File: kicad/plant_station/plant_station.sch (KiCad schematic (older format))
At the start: 20 parts, among them IC1 LP5024RSMR, IC2 VEML7700-TT, U1 NodeMCU2

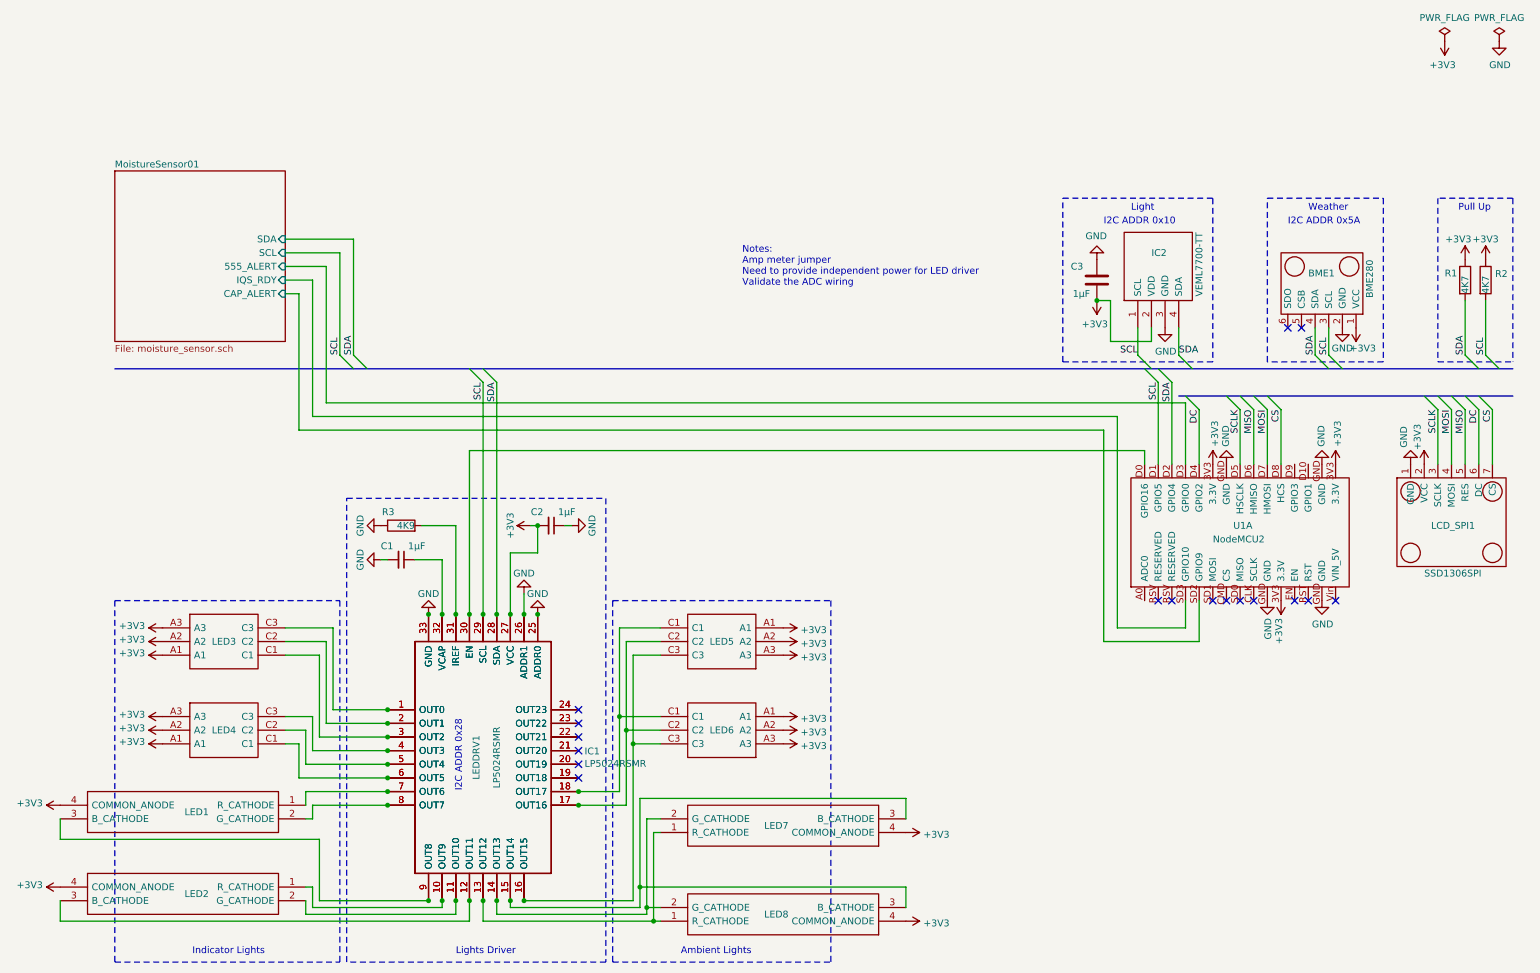
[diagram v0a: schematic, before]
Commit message: Board v.2 sent for printing
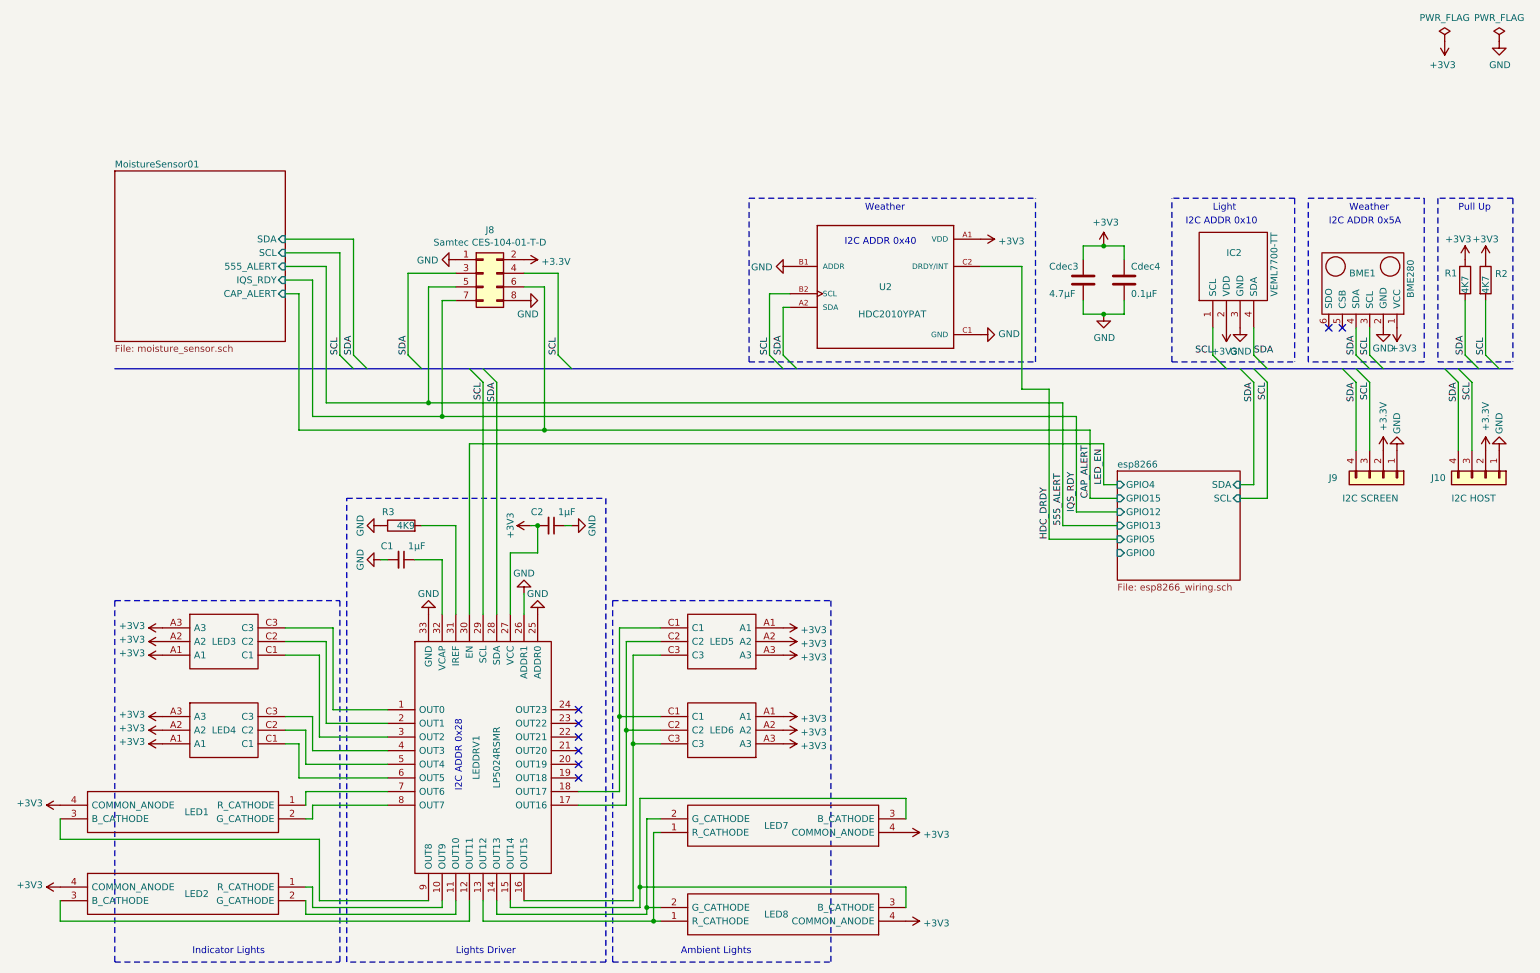
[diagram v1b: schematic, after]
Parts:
- removed C3: 1μF, symbol Device:C
- removed IC1: LP5024RSMR, SamacSys:QFN40P400X400X100-33N-D, symbol SamaSys:LP5024RSMR
- removed LCD_SPI1: SSD1306SPI, Connector_PinSocket_2.54mm:PinSocket_1x07_P2.54mm_Vertical, symbol LocalsLib:SSD1306SPI
- removed U1: NodeMCU2, symbol LocalsLib:NodeMCU2
- added Cdec3: 4.7μF, Capacitor_SMD:C_1206_3216Metric, symbol Device:C
- added Cdec4: 0.1μF, Capacitor_SMD:C_1206_3216Metric, symbol Device:C
- added J10: I2C HOST, Connector_PinSocket_2.54mm:PinSocket_1x04_P2.54mm_Vertical, symbol Connector_Generic:Conn_01x04
- added J8: Samtec CES-104-01-T-D, Connector_PinSocket_2.54mm:PinSocket_2x04_P2.54mm_Vertical, symbol Connector_Generic:Conn_02x04_Odd_Even
- added J9: I2C SCREEN, Connector_PinSocket_2.54mm:PinSocket_1x04_P2.54mm_Vertical, symbol Connector_Generic:Conn_01x04
- added U2: HDC2010YPAT, LocalsLib:BGA6C100X50P2X3_146X146X67, symbol HDC2010YPAT:HDC2010YPAT
- C1, C2: footprint Capacitor_SMD:C_1206_3216Metric_Pad1.42x1.75mm_HandSolder -> Capacitor_SMD:C_1206_3216Metric
- R1, R2, R3: footprint (none) -> Resistor_SMD:R_0805_2012Metric
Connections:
- net +3V3: now also Cdec3.1, Cdec4.1, J10.2 (Pin_2), J8.2 (Pin_2), J9.2 (Pin_2), U2.A1 (VDD)
- net GND: now also Cdec3.2, Cdec4.2, J10.1 (Pin_1), J8.1 (Pin_1), J8.8 (Pin_8), J9.1 (Pin_1), U2.B1 (ADDR), U2.C1 (GND)
- net SCL: now also J10.3 (Pin_3), J8.4 (Pin_4), J9.3 (Pin_3), U2.B2 (SCL)
- net SDA: now also J10.4 (Pin_4), J8.3 (Pin_3), J9.4 (Pin_4), U2.A2 (SDA)
- net LED_EN: now reaches LEDDRV1.30 (EN)
- new net 555_ALERT: J8.5 (Pin_5)
- new net CAP_ALERT: J8.6 (Pin_6)
- new net HDC_DRDY: U2.C2 (DRDY/INT)
- new net IQS_RDY: J8.7 (Pin_7)
- no-connect marks 17 -> 8
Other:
- note added: "I2C ADDR 0x40"
- note removed: "Notes: \nAmp meter jumper\nNeed to provide independent power for LED driver\nValidate the ADC wiring"
- moved on the sheet: BME1, IC2
